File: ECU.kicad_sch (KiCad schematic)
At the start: 124 parts, among them J1 Solenoid 0, J10 Thermocouple 3, J13 External SPI, J14 External UART, J15 External I2C, J16 Pressure Transducer 0, J17 Pressure Transducer 1, J18 Pressure Transducer 2, J19 Pressure Transducer 3, J2 Solenoid 1, J20 Pressure Transducer 4, J21 Pressure Transducer 5, J22 Power In, J3 Solenoid 2, J4 Solenoid 3, J5 Solenoid 4, J6 Solenoid 5, J7 Thermocouple 0, J8 Thermocouple 1, J9 Thermocouple 2, U1 Teensy4.1, U10 MAX31855, U11 MAX31855, U12 OPA357, U13 OPA357, U14 OPA357, U15 OPA357, U16 OPA357, U17 OPA357, U18 uA7824, U19 uA7824, U2 OPA357, U20 uA7805, U21 TLV2217, U3 OPA357, U4 OPA357, U5 OPA357, U6 OPA357, U7 OPA357, U8 MAX31855, U9 MAX31855

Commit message: Correct resistor part numbers
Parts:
- R27, R28: Part # Generic 4.7K 0603 Resistor -> Generic 1.2K 0603 Resistor
- R29: Part # Generic 4.7K 0603 Resistor -> Generic 150R 0603 Resistor
- R30: Part # Generic 4.7K 0603 Resistor -> Generic 68R 0603 Resistor
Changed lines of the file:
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@@
       (effects (font (size 1.27 1.27)) hide)
     )
-    (property "Datasheet" "" (id 3) (at 374.65 26.67 0)
+    (property "Datasheet" "~" (id 3) (at 374.65 26.67 0)
       (effects (font (size 1.27 1.27)) hide)
     )
@@
       (effects (font (size 1.27 1.27)) hide)
     )
-    (property "Datasheet" "" (id 3) (at 243.84 154.94 0)
+    (property "Datasheet" "~" (id 3) (at 243.84 154.94 0)
       (effects (font (size 1.27 1.27)) hide)
     )
@@
       (effects (font (size 1.27 1.27)) hide)
     )
-    (property "Part #" "Generic 4.7K 0603 Resistor" (id 5) (at 293.37 105.41 0)
+    (property "Part #" "Generic 1.2K 0603 Resistor" (id 5) (at 293.37 105.41 0)
       (effects (font (size 1.27 1.27)) hide)
     )
@@
       (effects (font (size 1.27 1.27)) hide)
     )
-    (property "Part #" "Generic 4.7K 0603 Resistor" (id 5) (at 307.34 105.41 0)
+    (property "Part #" "Generic 150R 0603 Resistor" (id 5) (at 307.34 105.41 0)
       (effects (font (size 1.27 1.27)) hide)
     )
@@
       (effects (font (size 1.27 1.27)) hide)
     )
-    (property "Datasheet" "" (id 3) (at 321.31 199.39 0)
+    (property "Datasheet" "~" (id 3) (at 321.31 199.39 0)
       (effects (font (size 1.27 1.27)) hide)
     )
@@
       (effects (font (size 1.27 1.27)) hide)
     )
-    (property "Datasheet" "" (id 3) (at 166.37 72.39 0)
+    (property "Datasheet" "~" (id 3) (at 166.37 72.39 0)
       (effects (font (size 1.27 1.27)) hide)
     )
@@
       (effects (font (size 1.27 1.27)) hide)
     )
-    (property "Datasheet" "" (id 3) (at 166.37 199.39 0)
+    (property "Datasheet" "~" (id 3) (at 166.37 199.39 0)
       (effects (font (size 1.27 1.27)) hide)
     )
@@
       (effects (font (size 1.27 1.27)) hide)
     )
-    (property "Datasheet" "" (id 3) (at 323.85 54.61 0)
+    (property "Datasheet" "~" (id 3) (at 323.85 54.61 0)
       (effects (font (size 1.27 1.27)) hide)
     )
@@
       (effects (font (size 1.27 1.27)) hide)
     )
-    (property "Datasheet" "" (id 3) (at 53.34 186.69 0)
+    (property "Datasheet" "~" (id 3) (at 53.34 186.69 0)
       (effects (font (size 1.27 1.27)) hide)
     )
@@
       (effects (font (size 1.27 1.27)) hide)
     )
-    (property "Datasheet" "" (id 3) (at 166.37 34.29 0)
+    (property "Datasheet" "~" (id 3) (at 166.37 34.29 0)
       (effects (font (size 1.27 1.27)) hide)
     )
@@
       (effects (font (size 1.27 1.27)) hide)
     )
-    (property "Datasheet" "" (id 3) (at 49.53 78.74 0)
+    (property "Datasheet" "~" (id 3) (at 49.53 78.74 0)
       (effects (font (size 1.27 1.27)) hide)
     )
@@
       (effects (font (size 1.27 1.27)) hide)
     )
-    (property "Datasheet" "" (id 3) (at 166.37 110.49 0)
+    (property "Datasheet" "~" (id 3) (at 166.37 110.49 0)
       (effects (font (size 1.27 1.27)) hide)
     )
@@
       (effects (font (size 1.27 1.27)) hide)
     )
-    (property "Datasheet" "" (id 3) (at 355.6 54.61 0)
+    (property "Datasheet" "~" (id 3) (at 355.6 54.61 0)
       (effects (font (size 1.27 1.27)) hide)
     )
@@
       (effects (font (size 1.27 1.27)) hide)
     )
-    (property "Part #" "Generic 4.7K 0603 Resistor" (id 5) (at 321.31 105.41 0)
+    (property "Part #" "Generic 68R 0603 Resistor" (id 5) (at 321.31 105.41 0)
       (effects (font (size 1.27 1.27)) hide)
     )
@@
       (effects (font (size 1.27 1.27)) hide)
     )
-    (property "Datasheet" "" (id 3) (at 323.85 26.67 0)
+    (property "Datasheet" "~" (id 3) (at 323.85 26.67 0)
       (effects (font (size 1.27 1.27)) hide)
     )
@@
       (effects (font (size 1.27 1.27)) hide)
     )
-    (property "Datasheet" "" (id 3) (at 53.34 143.51 0)
+    (property "Datasheet" "~" (id 3) (at 53.34 143.51 0)
       (effects (font (size 1.27 1.27)) hide)
     )
@@
       (effects (font (size 1.27 1.27)) hide)
     )
-    (property "Datasheet" "" (id 3) (at 243.84 34.29 0)
+    (property "Datasheet" "~" (id 3) (at 243.84 34.29 0)
       (effects (font (size 1.27 1.27)) hide)
     )
@@
       (effects (font (size 1.27 1.27)) hide)
     )
-    (property "Datasheet" "" (id 3) (at 166.37 154.94 0)
+    (property "Datasheet" "~" (id 3) (at 166.37 154.94 0)
       (effects (font (size 1.27 1.27)) hide)
     )
@@
       (effects (font (size 1.27 1.27)) hide)
     )
-    (property "Datasheet" "" (id 3) (at 243.84 110.49 0)
+    (property "Datasheet" "~" (id 3) (at 243.84 110.49 0)
       (effects (font (size 1.27 1.27)) hide)
     )
@@
       (effects (font (size 1.27 1.27)) hide)
     )
-    (property "Datasheet" "" (id 3) (at 53.34 208.28 0)
+    (property "Datasheet" "~" (id 3) (at 53.34 208.28 0)
       (effects (font (size 1.27 1.27)) hide)
     )
@@
       (effects (font (size 1.27 1.27)) hide)
     )
-    (property "Datasheet" "" (id 3) (at 321.31 154.94 0)
+    (property "Datasheet" "~" (id 3) (at 321.31 154.94 0)
       (effects (font (size 1.27 1.27)) hide)
     )
@@
       (effects (font (size 1.27 1.27)) hide)
     )
-    (property "Datasheet" "" (id 3) (at 243.84 199.39 0)
+    (property "Datasheet" "~" (id 3) (at 243.84 199.39 0)
       (effects (font (size 1.27 1.27)) hide)
     )
@@
       (effects (font (size 1.27 1.27)) hide)
     )
-    (property "Datasheet" "" (id 3) (at 243.84 72.39 0)
+    (property "Datasheet" "~" (id 3) (at 243.84 72.39 0)
       (effects (font (size 1.27 1.27)) hide)
     )
@@
       (effects (font (size 1.27 1.27)) hide)
     )
-    (property "Datasheet" "" (id 3) (at 53.34 165.1 0)
+    (property "Datasheet" "~" (id 3) (at 53.34 165.1 0)
       (effects (font (size 1.27 1.27)) hide)
     )
@@
       (effects (font (size 1.27 1.27)) hide)
     )
-    (property "Part #" "Generic 4.7K 0603 Resistor" (id 5) (at 279.4 105.41 0)
+    (property "Part #" "Generic 1.2K 0603 Resistor" (id 5) (at 279.4 105.41 0)
       (effects (font (size 1.27 1.27)) hide)
     )

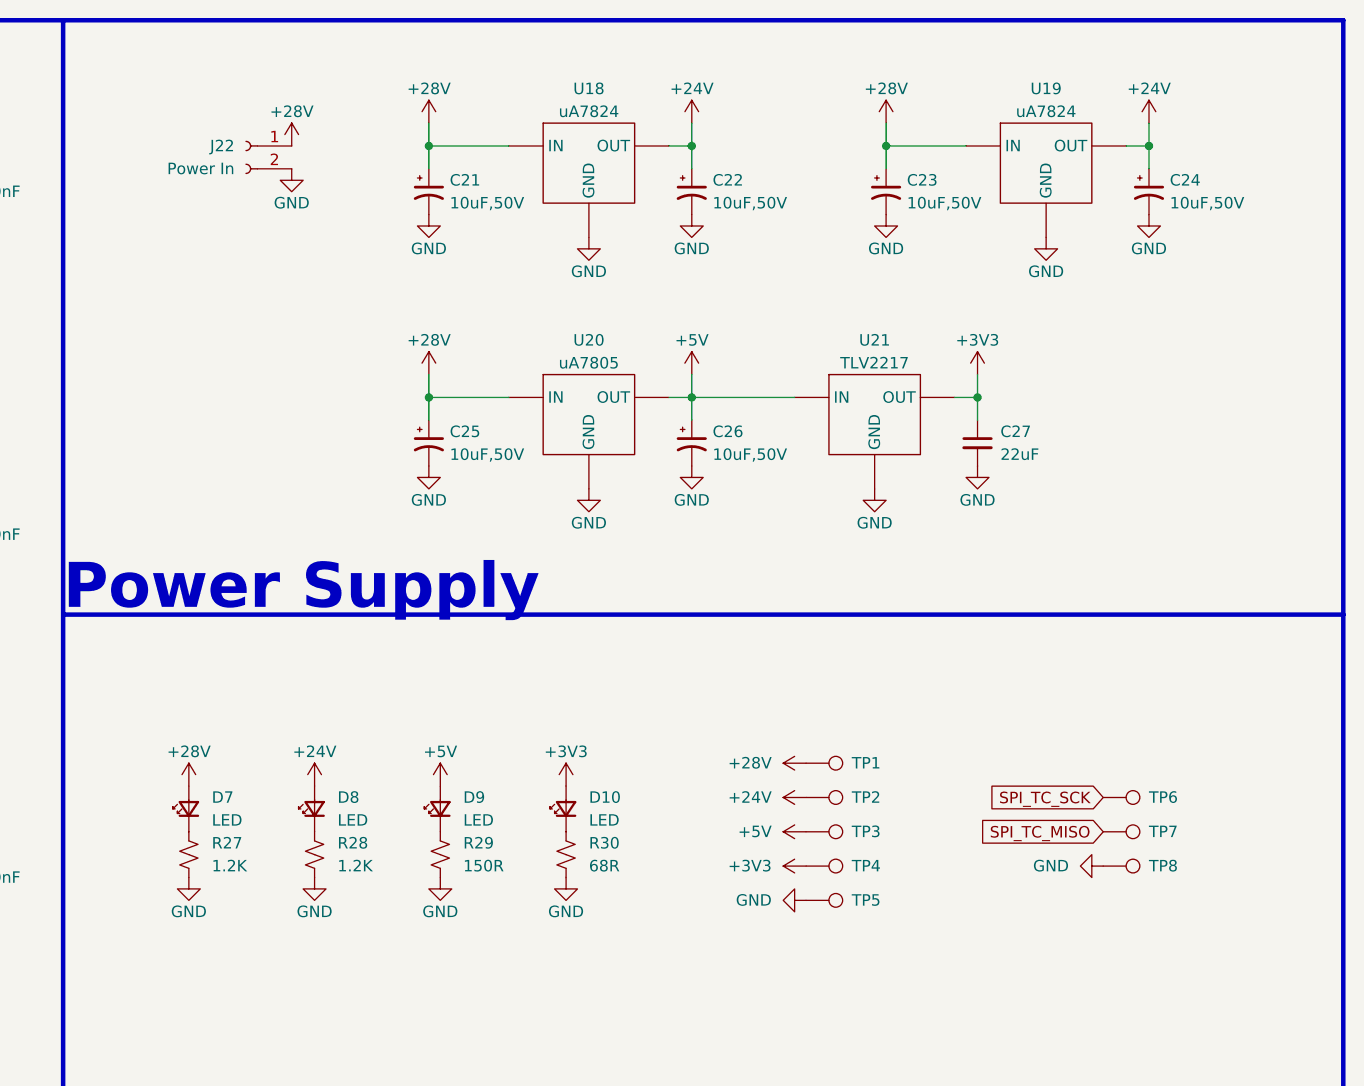
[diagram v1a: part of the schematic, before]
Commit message: Redesign power supply
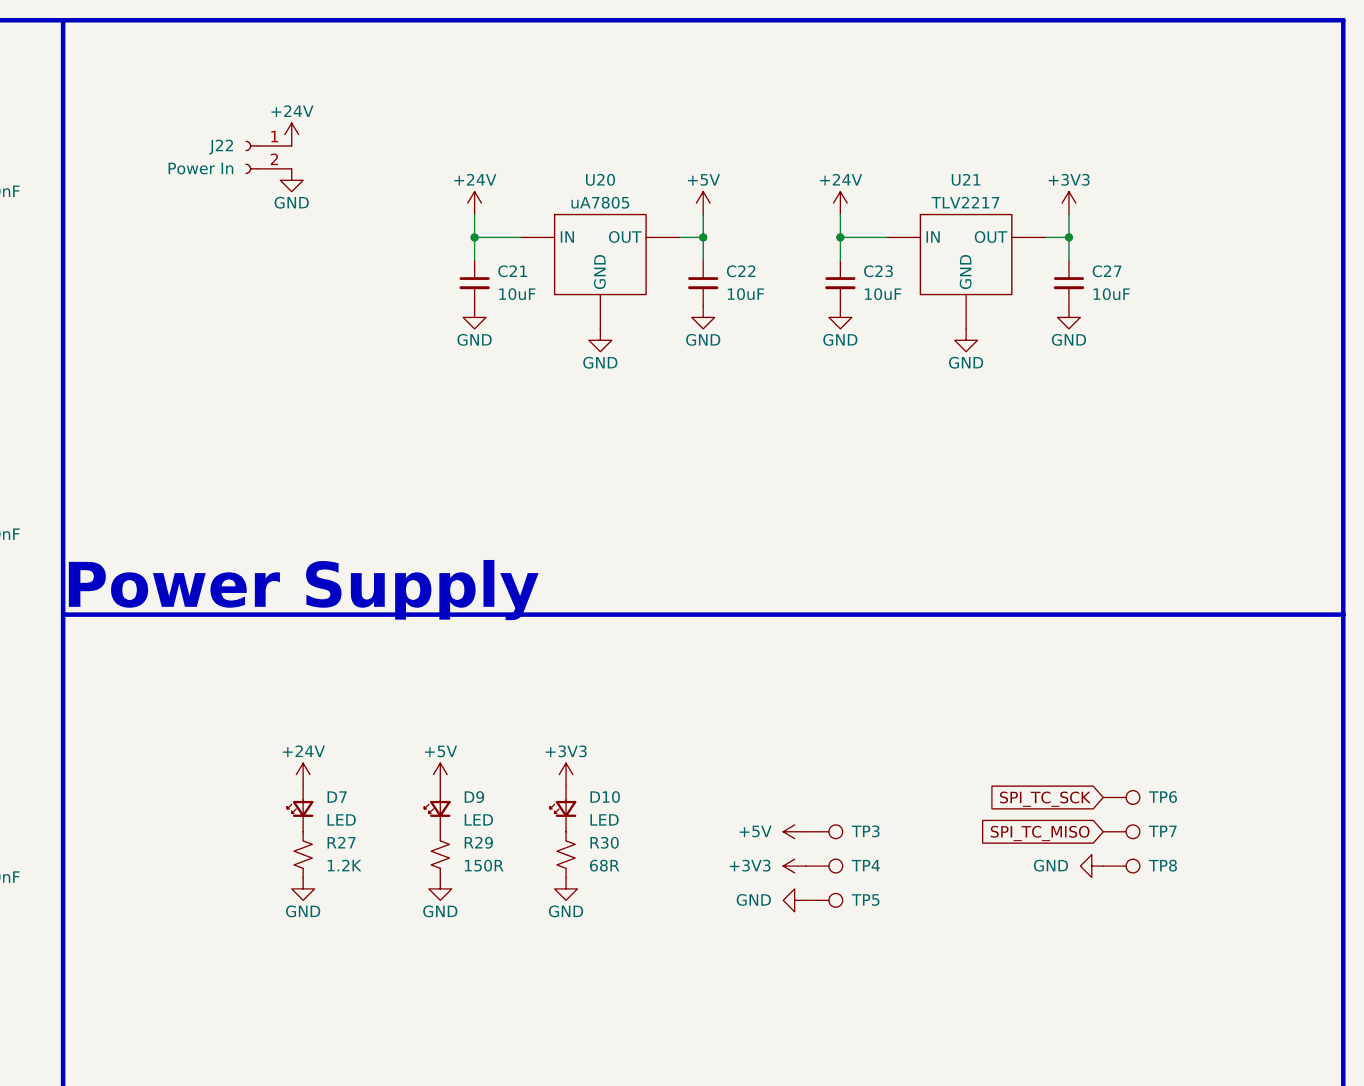
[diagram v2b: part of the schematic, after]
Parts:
- removed C21, C22, C23, C24, C25, C26: 10uF,50V, Capacitor_SMD:CP_Elec_5x5.9, symbol Device:C_Polarized_Small_US
- removed D8: LED, Diode_SMD:D_0603_1608Metric, symbol Device:LED_Small
- removed R28: 1.2K, Resistor_SMD:R_0603_1608Metric, symbol Device:R_Small_US
- removed TP1, TP2: ~, TestPoint:TestPoint_Pad_D4.0mm, symbol Connector:TestPoint
- removed U18, U19: uA7824, Package_TO_SOT_THT:TO-220-3_Vertical, symbol ECU:uA78xx
- added C21, C22, C23: 10uF, Capacitor_SMD:C_1206_3216Metric, symbol Device:C_Small
- C27: value 22uF -> 10uF; footprint Capacitor_SMD:C_0805_2012Metric -> Capacitor_SMD:C_1206_3216Metric; Part # Generic 22uF 0805 MLCC -> Generic 10uF 1206 MLCC
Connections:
- net +28V is gone; now on net +24V: D7.2 (A), J22.1 (Pin_1), U20.1 (IN)
- net +24V: now also U21.1 (IN), C21.1, C23.1
- net +5V: now also C22.1; no longer U21.1 (IN)
- net GND: now also C21.2, C22.2, C23.2
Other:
- moved on the sheet: C27, D7, R27, U20, U21

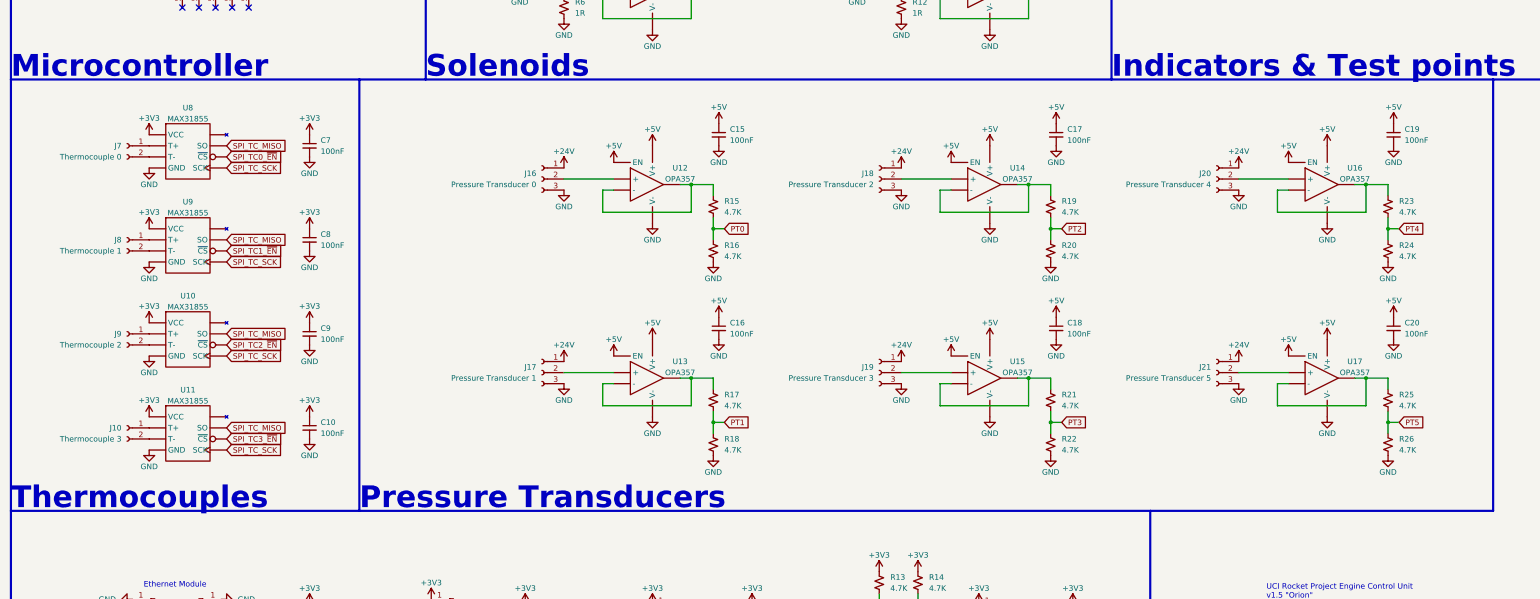
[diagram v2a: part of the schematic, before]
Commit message: Add filter caps to TC input
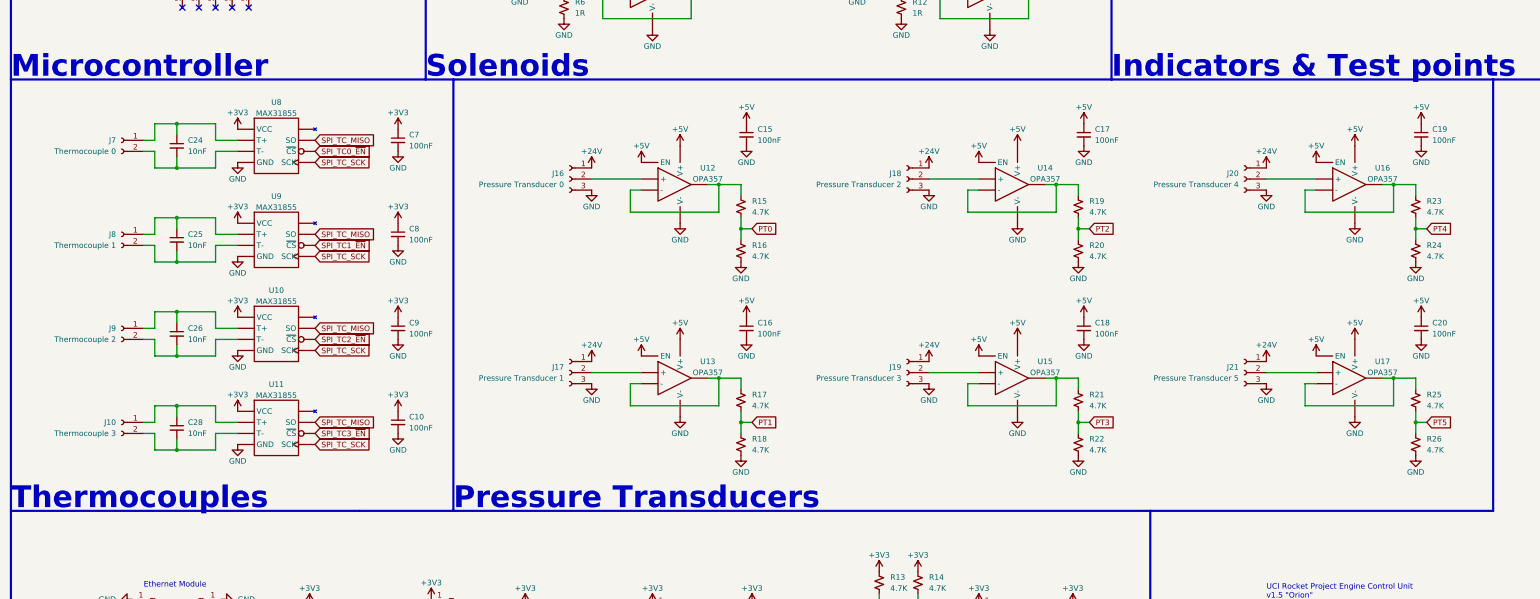
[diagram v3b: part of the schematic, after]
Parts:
- added C24, C25, C26, C28: 10nF, Capacitor_SMD:C_0603_1608Metric, symbol Device:C_Small
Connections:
- net at J9.2 (Pin_2), U10.2 (T-): now also C26.2
- net at J9.1 (Pin_1), U10.3 (T+): now also C26.1
- net at J7.1 (Pin_1), U8.3 (T+): now also C24.1
- net at J7.2 (Pin_2), U8.2 (T-): now also C24.2
- net at J10.1 (Pin_1), U11.3 (T+): now also C28.1
- net at J10.2 (Pin_2), U11.2 (T-): now also C28.2
- net at J8.1 (Pin_1), U9.3 (T+): now also C25.1
- net at J8.2 (Pin_2), U9.2 (T-): now also C25.2
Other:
- moved on the sheet: C10, C15, C16, C17, C18, C19, C20, C7, C8, C9, J10, J16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
